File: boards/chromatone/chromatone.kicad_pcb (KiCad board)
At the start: 2 copper layers, 50 x 50 mm, 0 parts

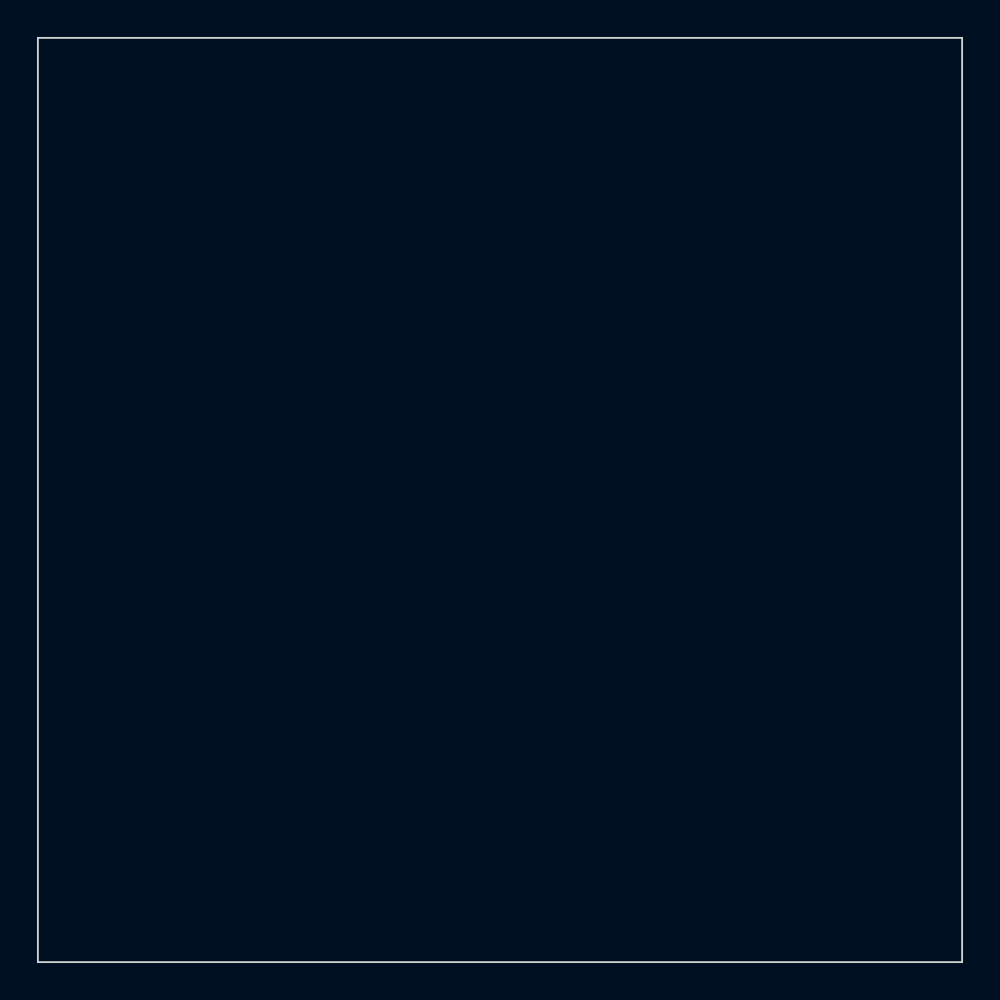
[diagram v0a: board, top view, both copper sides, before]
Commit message: chromatone: PCB layout rev A (46x30 mm, split ground pours, 3 mm barrier) + generators
DRC clean with warnings and schematic parity; make jlcpcb runs end to end.

Co-Authored-By: Claude Fable 5.1 <noreply@anthropic.com>
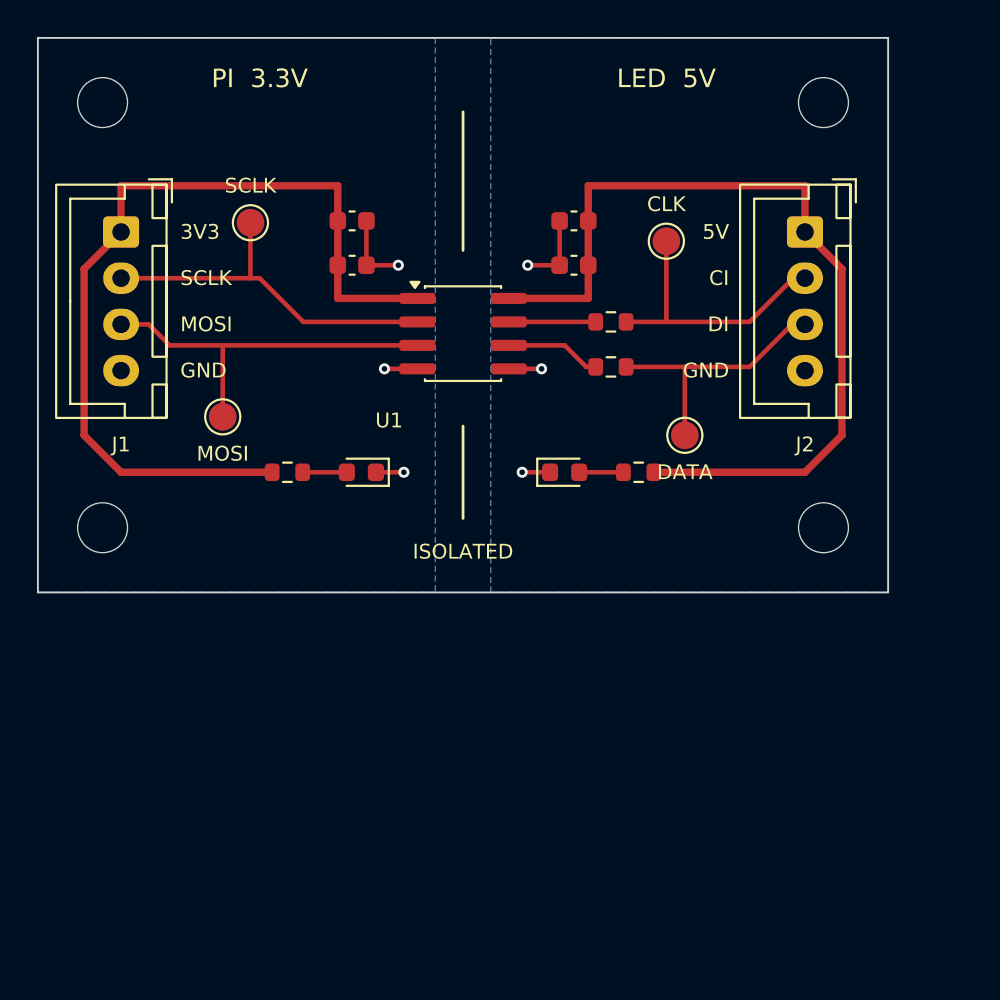
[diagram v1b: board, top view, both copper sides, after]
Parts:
- added C1: 100n, Capacitor_SMD:C_0603_1608Metric, F.Cu at (67.0, 62.3)
- added C2: 10u, Capacitor_SMD:C_0603_1608Metric, F.Cu at (67.0, 59.9)
- added C3: 100n, Capacitor_SMD:C_0603_1608Metric, F.Cu at (79.0, 62.3)
- added C4: 10u, Capacitor_SMD:C_0603_1608Metric, F.Cu at (79.0, 59.9)
- added D1: GREEN, LED_SMD:LED_0603_1608Metric, F.Cu at (67.5, 73.5)
- added D2: BLUE, LED_SMD:LED_0603_1608Metric, F.Cu at (78.5, 73.5)
- added H1: M2.5, MountingHole:MountingHole_2.7mm_M2.5, F.Cu at (53.5, 53.5)
- added H2: M2.5, MountingHole:MountingHole_2.7mm_M2.5, F.Cu at (92.5, 53.5)
- added H3: M2.5, MountingHole:MountingHole_2.7mm_M2.5, F.Cu at (53.5, 76.5)
- added H4: M2.5, MountingHole:MountingHole_2.7mm_M2.5, F.Cu at (92.5, 76.5)
- added J1: Pi SPI, Connector_JST:JST_XH_B4B-XH-A_1x04_P2.50mm_Vertical, F.Cu at (54.5, 60.5)
- added J2: Strip, Connector_JST:JST_XH_B4B-XH-A_1x04_P2.50mm_Vertical, F.Cu at (91.5, 60.5)
- added R1: 47, Resistor_SMD:R_0603_1608Metric, F.Cu at (81.0, 65.4)
- added R2: 47, Resistor_SMD:R_0603_1608Metric, F.Cu at (81.0, 67.8)
- added R3: 1k, Resistor_SMD:R_0603_1608Metric, F.Cu at (63.5, 73.5)
- added R4: 1k, Resistor_SMD:R_0603_1608Metric, F.Cu at (82.5, 73.5)
- added TP1: SCLK, TestPoint:TestPoint_Pad_D1.5mm, F.Cu at (61.5, 60.0)
- added TP2: MOSI, TestPoint:TestPoint_Pad_D1.5mm, F.Cu at (60.0, 70.5)
- added TP3: CLK, TestPoint:TestPoint_Pad_D1.5mm, F.Cu at (84.0, 61.0)
- added TP4: DATA, TestPoint:TestPoint_Pad_D1.5mm, F.Cu at (85.0, 71.5)
- added U1: ISO7720D, Package_SO:SOIC-8_3.9x4.9mm_P1.27mm, F.Cu at (73.0, 66.0)
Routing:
- net +5V_LED: track 0.00 -> 47.5 mm
- net +3V3: track 0.00 -> 47.5 mm
- net Net-(J1-Pin_3): track 0.00 -> 20.4 mm
- net Net-(J1-Pin_2): track 0.00 -> 20.0 mm
- net Net-(J2-Pin_2): track 0.00 -> 15.0 mm
- net Net-(J2-Pin_3): track 0.00 -> 14.3 mm
- net GND_LED: track 0.00 -> 7.41 mm, vias 0 -> 3
- net GND: track 0.00 -> 7.41 mm, vias 0 -> 3
- net Net-(U1-OUTB): track 0.00 -> 5.18 mm
- net Net-(U1-OUTA): track 0.00 -> 4.70 mm
- net Net-(D2-A): track 0.00 -> 2.39 mm
- net Net-(D1-A): track 0.00 -> 2.39 mm
- added copper zone on B.Cu, net GND
- added copper zone on B.Cu, net GND_LED
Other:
- board size 50 x 50 mm -> 46 x 30 mm
- board text added: "3V3"
- board text added: "5V"
- board text added: "CI"
- board text added: "DI"
- board text added: "GND"
- board text added: "ISOLATED"
- board text added: "LED 5V"
- board text added: "MOSI"
- board text added: "PI 3.3V"
- board text added: "SCLK"
- board text added: "chromatone rev A"

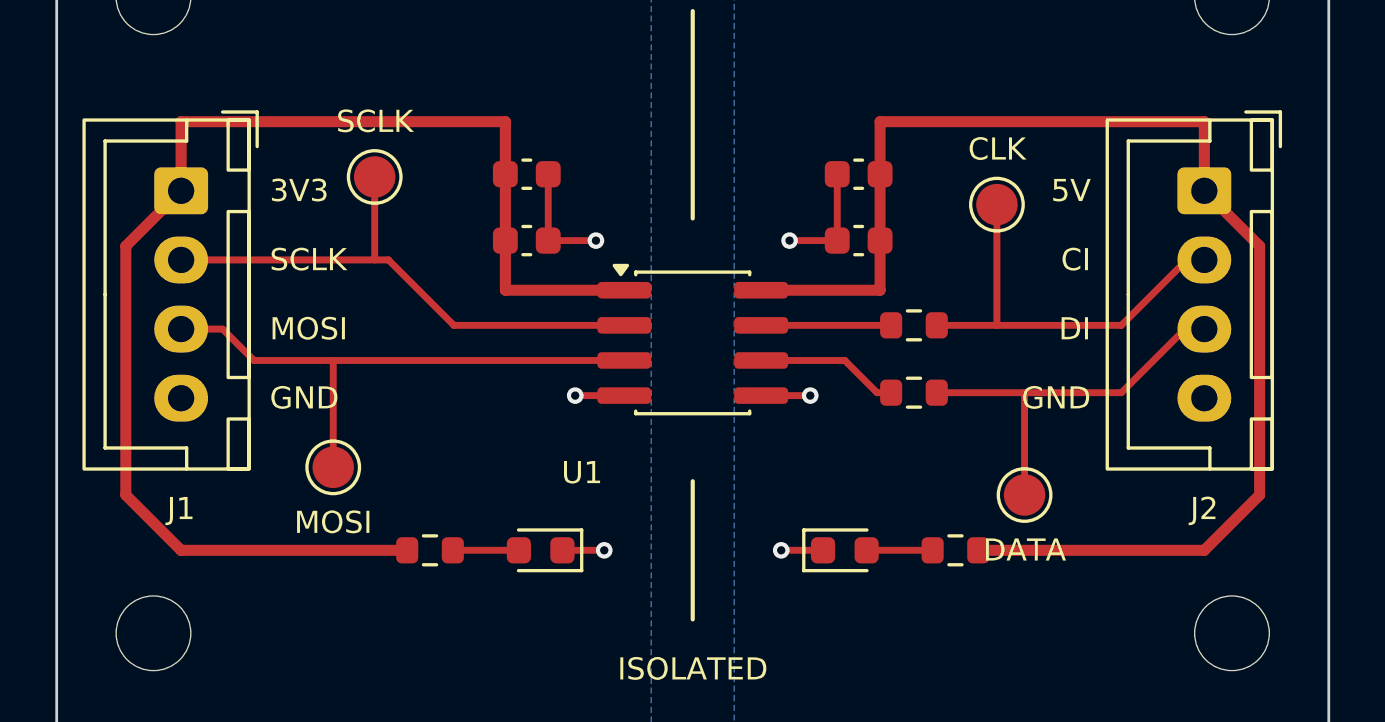
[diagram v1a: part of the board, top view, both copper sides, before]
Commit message: chromatone: review fixes (JST LCSC C144395, decoupling at U1 pins, hole keepouts, ground test pads, 8 MHz target)
Co-Authored-By: Claude Fable 5.1 <noreply@anthropic.com>
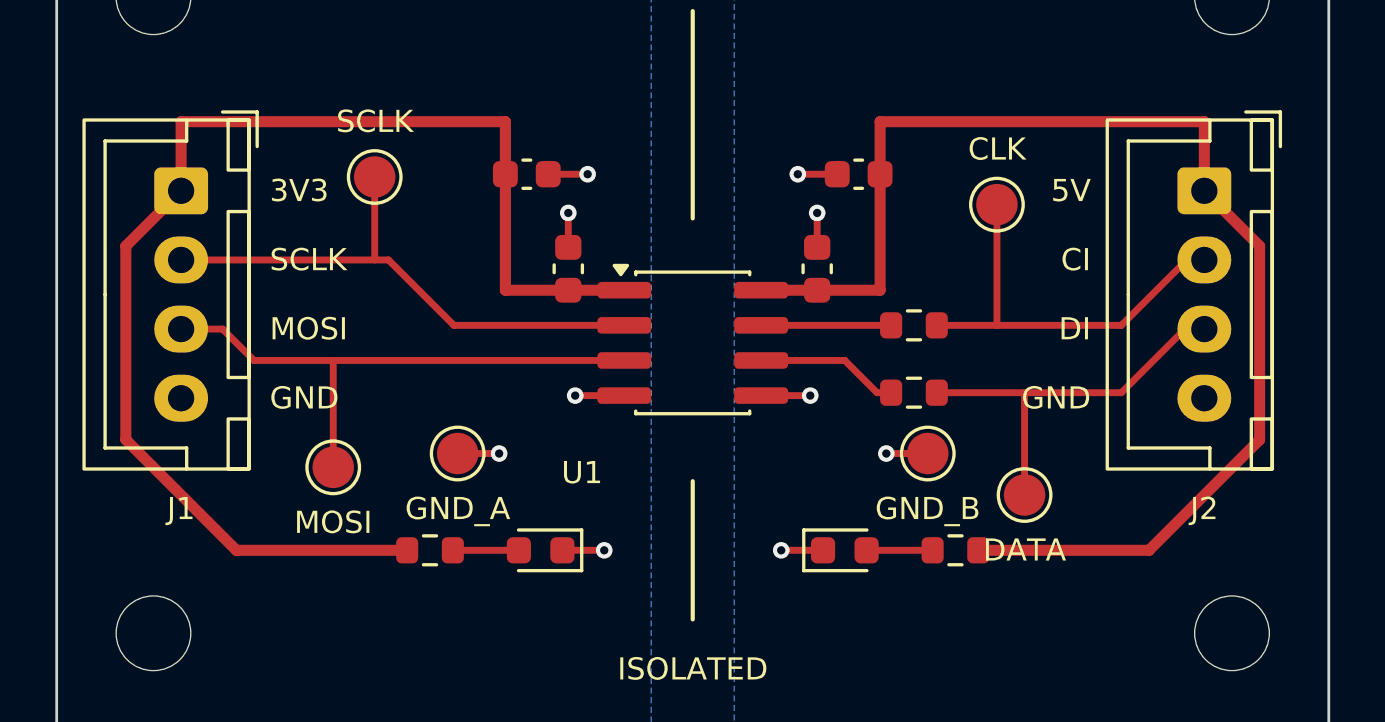
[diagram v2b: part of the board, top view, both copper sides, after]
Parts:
- added TP5: GND_A, TestPoint:TestPoint_Pad_D1.5mm, F.Cu at (64.5, 70.0)
- added TP6: GND_B, TestPoint:TestPoint_Pad_D1.5mm, F.Cu at (81.5, 70.0)
- moved C1 1.81 mm to (68.5, 63.3), turned to 90 degrees
- moved C3 1.81 mm to (77.5, 63.3), turned to 90 degrees
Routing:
- net +3V3: track 47.5 -> 46.3 mm
- net +5V_LED: track 47.5 -> 46.3 mm
- net GND_LED: track 7.41 -> 7.46 mm, vias 3 -> 5
- net GND: track 7.41 -> 7.46 mm, vias 3 -> 5
